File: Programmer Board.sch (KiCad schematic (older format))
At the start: 7 parts, among them J1 105-1103-001, J10 Conn_01x03, J11 105-1102-001, J12 105-1103-001, J2 Conn_01x03, J3 105-1102-001, J9 Conn_02x18_Odd_Even

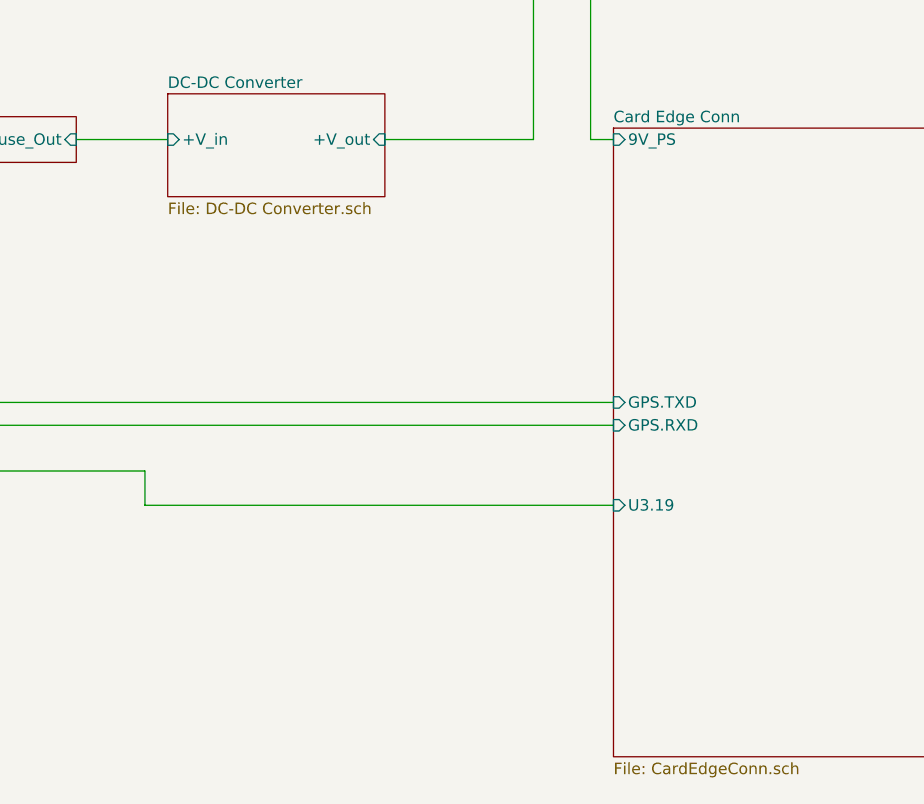
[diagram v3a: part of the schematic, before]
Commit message: Fixed DRC Errors
Fixed drc errors
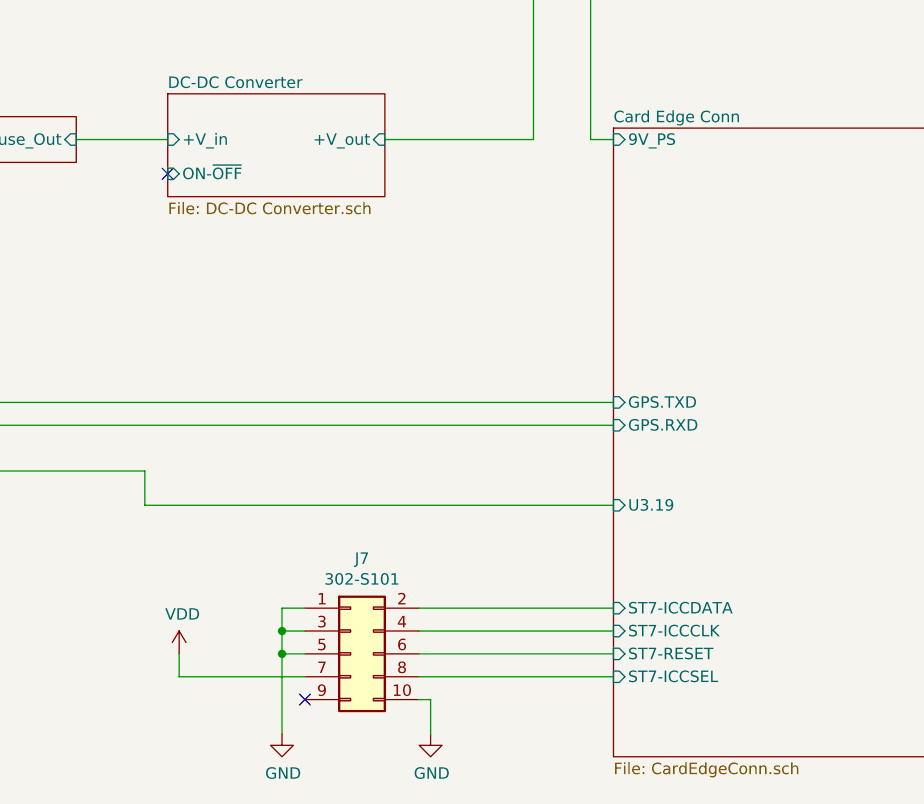
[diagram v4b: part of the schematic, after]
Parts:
- added J7: 302-S101, digikey-footprints:PinHeader_2x5_P2.54mm_Drill1.2mm, symbol Connector_Generic:Conn_02x05_Odd_Even
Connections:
- net GND: now also J7.1 (Pin_1), J7.10 (Pin_10), J7.3 (Pin_3), J7.5 (Pin_5)
- new net Card Edge Conn/ST7-ICCCLK: J7.4 (Pin_4)
- new net Card Edge Conn/ST7-ICCDATA: J7.2 (Pin_2)
- new net Card Edge Conn/ST7-ICCSEL: J7.8 (Pin_8)
- new net Card Edge Conn/ST7-RESET: J7.6 (Pin_6)
- new net VDD: J7.7 (Pin_7)
- no-connect marks 0 -> 2
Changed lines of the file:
@@
 Title "LMS6 Interface Board"
 Date "2020-10-17"
-Rev "6"
+Rev "7"
 Comp ""
-Comment1 "Rev 3: Changed sheet to US Letter"
-Comment2 "Rev 4: Fixed J9 hanging over border of sheet."
-Comment3 "Rev 5: Fixed J6 footprint and MPN info."
-Comment4 "Rev 6: Fixed footprint issues. Changed J9 connections for layout. Changed Y1."
+Comment1 "Rev 4: Fixed J9 hanging over border of sheet."
+Comment2 "Rev 5: Fixed J6 footprint and MPN info."
+Comment3 "Rev 6: Fixed footprint issues. Changed J9 connections for layout. Changed Y1."
+Comment4 "Rev 7: Ran DRC and fixed errors with flags to make rixon happy."
 $EndDescr
 $Sheet
@@
 F2 "+V_in" I L 4800 3300 50
 F3 "+V_out" I R 5750 3300 50
+F4 "ON-~OFF" I L 4800 3450 50
 $EndSheet
 $Comp
@@
 F22 "HEADER1.10" I R 9450 3600 50
 F23 "9V_PS" I L 6750 3300 50
+F24 "ST7-ICCSEL" I L 6750 5650 50
+F25 "ST7-ICCDATA" I L 6750 5350 50
+F26 "ST7-RESET" I L 6750 5550 50
+F27 "ST7-ICCCLK" I L 6750 5450 50
 $EndSheet
 Wire Wire Line
@@
 Text Label 900  3200 0    50   ~ 0
 -PS
+NoConn ~ 4800 3450
+$Comp
+L Connector_Generic:Conn_02x05_Odd_Even J?
+U 1 1 5F9DEBE9
+P 5600 5550
+AR Path="/5F7C6408/5F9DEBE9" Ref="J?"  Part="1"
+AR Path="/5F9DEBE9" Ref="J7"  Part="1"
+F 0 "J7" H 5650 5967 50  0000 C CNN
+F 1 "302-S101" H 5650 5876 50  0000 C CNN
+F 2 "digikey-footprints:PinHeader_2x5_P2.54mm_Drill1.2mm" H 5600 5550 50  0001 C CNN
+F 3 "http://www.on-shore.com/wp-content/uploads/2018/04/302-SXX1.pdf" H 5600 5550 50  0001 C CNN
+F 4 "302-S101" H 5600 5550 50  0001 C CNN "MPN"
+F 5 "On Shore Technology Inc." H 5600 5550 50  0001 C CNN "Maufacturer"
+	1    5600 5550
+	1    0    0    -1
+$EndComp
+$Comp
+L power:VDD #PWR0108
+U 1 1 5F9DEBF3
+P 4850 5550
+AR Path="/5F9DEBF3" Ref="#PWR0108"  Part="1"
+AR Path="/5F7BE189/5F9DEBF3" Ref="#PWR?"  Part="1"
+AR Path="/5F7C6408/5F9DEBF3" Ref="#PWR?"  Part="1"
+F 0 "#PWR0108" H 4850 5400 50  0001 C CNN
+F 1 "VDD" H 4865 5723 50  0000 C CNN
+F 2 "" H 4850 5550 50  0001 C CNN
+F 3 "" H 4850 5550 50  0001 C CNN
+	1    4850 5550
+	1    0    0    -1
+$EndComp
+Wire Wire Line
+	5400 5650 4850 5650
+Wire Wire Line
+	4850 5650 4850 5550
+$Comp
+L power:GND #PWR0109
+U 1 1 5F9DEBFB
+P 5300 5900
+AR Path="/5F9DEBFB" Ref="#PWR0109"  Part="1"
+AR Path="/5F7BE189/5F9DEBFB" Ref="#PWR?"  Part="1"
+AR Path="/5F7C6408/5F9DEBFB" Ref="#PWR?"  Part="1"
+F 0 "#PWR0109" H 5300 5650 50  0001 C CNN
+F 1 "GND" H 5305 5727 50  0000 C CNN
+F 2 "" H 5300 5900 50  0001 C CNN
+F 3 "" H 5300 5900 50  0001 C CNN
+	1    5300 5900
+	1    0    0    -1
+$EndComp
+Wire Wire Line
+	5300 5350 5400 5350
+Wire Wire Line
+	5300 5350 5300 5450
+Wire Wire Line
+	5400 5550 5300 5550
+Connection ~ 5300 5550
+Wire Wire Line
+	5300 5550 5300 5900
+Wire Wire Line
+	5400 5450 5300 5450
+Connection ~ 5300 5450
+Wire Wire Line
+	5300 5450 5300 5550
+$Comp
+L power:GND #PWR0110
+U 1 1 5F9DEC09
+P 5950 5900
+AR Path="/5F9DEC09" Ref="#PWR0110"  Part="1"
+AR Path="/5F7BE189/5F9DEC09" Ref="#PWR?"  Part="1"
+AR Path="/5F7C6408/5F9DEC09" Ref="#PWR?"  Part="1"
+F 0 "#PWR0110" H 5950 5650 50  0001 C CNN
+F 1 "GND" H 5955 5727 50  0000 C CNN
+F 2 "" H 5950 5900 50  0001 C CNN
+F 3 "" H 5950 5900 50  0001 C CNN
+	1    5950 5900
+	1    0    0    -1
+$EndComp
+Wire Wire Line
+	5900 5750 5950 5750
+Wire Wire Line
+	5950 5750 5950 5900
+NoConn ~ 5400 5750
+Wire Wire Line
+	5900 5350 6750 5350
+Wire Wire Line
+	5900 5450 6750 5450
+Wire Wire Line
+	5900 5550 6750 5550
+Wire Wire Line
+	5900 5650 6750 5650
 $EndSCHEMATC

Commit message: Final updates to REV B
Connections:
- net Card Edge Conn/HEADER1.1: now also J9.5 (Pin_5); no longer J9.31 (Pin_31)
- net Card Edge Conn/HEADER1.10: now also J9.35 (Pin_35); no longer J9.3 (Pin_3)
- net Card Edge Conn/HEADER1.2: now also J9.13 (Pin_13); no longer J9.23 (Pin_23)
- net Card Edge Conn/HEADER1.3: now also J9.15 (Pin_15); no longer J9.21 (Pin_21)
- net Card Edge Conn/HEADER1.4: now also J9.19 (Pin_19); no longer J9.15 (Pin_15)
- net Card Edge Conn/HEADER1.5: now also J9.17 (Pin_17); no longer J9.19 (Pin_19)
- net Card Edge Conn/HEADER1.6: now also J9.21 (Pin_21); no longer J9.17 (Pin_17)
- net Card Edge Conn/HEADER1.7: now also J9.25 (Pin_25); no longer J9.11 (Pin_11)
- net Card Edge Conn/HEADER1.9: now also J9.31 (Pin_31); no longer J9.7 (Pin_7)
- net Card Edge Conn/J5.2: now also J9.3 (Pin_3); no longer J9.35 (Pin_35)
- net Card Edge Conn/J5.3: now also J9.27 (Pin_27); no longer J9.9 (Pin_9)
- net Card Edge Conn/SW1.1: now also J9.9 (Pin_9); no longer J9.25 (Pin_25)
- net Card Edge Conn/SW1.2: now also J9.11 (Pin_11); no longer J9.27 (Pin_27)
- net Card Edge Conn/SW1.3: now also J9.29 (Pin_29); no longer J9.5 (Pin_5)
- net Card Edge Conn/SW1.4: now also J9.7 (Pin_7); no longer J9.29 (Pin_29)
- net Card Edge Conn/U21.20-DCLK: now also J9.1 (Pin_1); no longer J9.33 (Pin_33)
- net Card Edge Conn/U22.3: now also J9.23 (Pin_23); no longer J9.13 (Pin_13)
- net Card Edge Conn/U3.18: now also J9.33 (Pin_33); no longer J9.1 (Pin_1)
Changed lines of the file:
@@
 Title "LMS6 Interface Board"
 Date "2020-10-17"
-Rev "7"
+Rev "9"
 Comp ""
-Comment1 "Rev 4: Fixed J9 hanging over border of sheet."
-Comment2 "Rev 5: Fixed J6 footprint and MPN info."
-Comment3 "Rev 6: Fixed footprint issues. Changed J9 connections for layout. Changed Y1."
-Comment4 "Rev 7: Ran DRC and fixed errors with flags to make rixon happy."
+Comment1 "Rev 6: Fixed footprint issues. Changed J9 connections for layout. Changed Y1."
+Comment2 "Rev 7: Ran DRC and fixed errors with flags to make rixon happy."
+Comment3 "Rev 8: J5 changed to edge connector"
+Comment4 "Rev 9: J9 Modified to help with routing."
 $EndDescr
 $Sheet
@@
 F0 "Card Edge Conn" 50
 F1 "CardEdgeConn.sch" 50
-F2 "U21.20-DCLK" I R 9450 5100 50
-F3 "SW1.1" I R 9450 4700 50
+F2 "U21.20-DCLK" I R 9450 5200 50
+F3 "SW1.1" I R 9450 4800 50
 F4 "GPS.TXD" I L 6750 4450 50
 F5 "U22.3" I R 9450 4100 50
 F6 "J5.3" I R 9450 3900 50
-F7 "SW1.3" I R 9450 3700 50
-F8 "U3.18" I R 9450 3500 50
+F7 "SW1.3" I R 9450 3800 50
+F8 "U3.18" I R 9450 3600 50
 F9 "GPS.RXD" I L 6750 4550 50
 F10 "U3.19" I L 6750 4900 50
-F11 "SW1.2" I R 9450 4800 50
+F11 "SW1.2" I R 9450 4700 50
 F12 "SW1.4" I R 9450 4900 50
-F13 "J5.2" I R 9450 5200 50
+F13 "J5.2" I R 9450 5100 50
 F14 "HEADER1.1" I R 9450 5000 50
 F15 "HEADER1.2" I R 9450 4600 50
 F16 "HEADER1.3" I R 9450 4500 50
-F17 "HEADER1.4" I R 9450 4200 50
+F17 "HEADER1.4" I R 9450 4300 50
 F18 "HEADER1.5" I R 9450 4400 50
-F19 "HEADER1.6" I R 9450 4300 50
+F19 "HEADER1.6" I R 9450 4200 50
 F20 "HEADER1.7" I R 9450 4000 50
-F21 "HEADER1.9" I R 9450 3800 50
-F22 "HEADER1.10" I R 9450 3600 50
+F21 "HEADER1.9" I R 9450 3700 50
+F22 "HEADER1.10" I R 9450 3500 50
 F23 "9V_PS" I L 6750 3300 50
 F24 "ST7-ICCSEL" I L 6750 5650 50
@@
 L Connector_Generic:Conn_02x18_Odd_Even J9
 U 1 1 5F8F3B51
-P 9850 4300
-F 0 "J9" H 9900 5317 50  0000 C CNN
-F 1 "Conn_02x18_Odd_Even" H 9900 5226 50  0000 C CNN
-F 2 "Connector_PinHeader_2.54mm:PinHeader_2x18_P2.54mm_Vertical" H 9850 4300 50  0001 C CNN
-F 3 "https://drawings-pdf.s3.amazonaws.com/11636.pdf" H 9850 4300 50  0001 C CNN
-F 4 "Sullins Connector Solutions" H 9850 4300 50  0001 C CNN "Manufacturer"
-F 5 "PREC020DAAN-RC" H 9850 4300 50  0001 C CNN "MPN"
-	1    9850 4300
-	1    0    0    -1
+P 9850 4400
+F 0 "J9" H 9900 5417 50  0000 C CNN
+F 1 "Conn_02x18_Odd_Even" H 9900 5326 50  0000 C CNN
+F 2 "Connector_PinHeader_2.54mm:PinHeader_2x18_P2.54mm_Vertical" H 9850 4400 50  0001 C CNN
+F 3 "https://drawings-pdf.s3.amazonaws.com/11636.pdf" H 9850 4400 50  0001 C CNN
+F 4 "Sullins Connector Solutions" H 9850 4400 50  0001 C CNN "Manufacturer"
+F 5 "PREC020DAAN-RC" H 9850 4400 50  0001 C CNN "MPN"
+	1    9850 4400
+	1    0    0    1
 $EndComp
 $Comp
@@
 	5900 2350 5900 1350
 Wire Wire Line
-	9450 3500 9650 3500
-Wire Wire Line
-	9450 3600 9650 3600
-Wire Wire Line
 	9450 3700 9650 3700
 Wire Wire Line
@@
 Wire Wire Line
 	5900 5650 6750 5650
+Wire Wire Line
+	9450 3500 9650 3500
+Wire Wire Line
+	9450 3600 9650 3600
 $EndSCHEMATC

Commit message: Added product info and Schematic
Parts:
- J9: MPN PREC020DAAN-RC -> PREC018DAAN-RC
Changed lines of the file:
@@
 Title "LMS6 Interface Board"
 Date "2020-10-17"
-Rev "9"
+Rev "10"
 Comp ""
-Comment1 "Rev 6: Fixed footprint issues. Changed J9 connections for layout. Changed Y1."
-Comment2 "Rev 7: Ran DRC and fixed errors with flags to make rixon happy."
-Comment3 "Rev 8: J5 changed to edge connector"
-Comment4 "Rev 9: J9 Modified to help with routing."
+Comment1 "Rev 7: Ran DRC and fixed errors with flags to make rixon happy."
+Comment2 "Rev 8: J5 changed to edge connector"
+Comment3 "Rev 9: J9 Modified to help with routing."
+Comment4 "10/22/2020 Rev 10: Updated U3 part number and Manufact props"
 $EndDescr
 $Sheet
@@
 F 3 "https://drawings-pdf.s3.amazonaws.com/11636.pdf" H 9850 4400 50  0001 C CNN
 F 4 "Sullins Connector Solutions" H 9850 4400 50  0001 C CNN "Manufacturer"
-F 5 "PREC020DAAN-RC" H 9850 4400 50  0001 C CNN "MPN"
+F 5 "PREC018DAAN-RC" H 9850 4400 50  0001 C CNN "MPN"
 	1    9850 4400
 	1    0    0    1

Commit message: Rev C Board layout
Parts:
- added D2: LG R971-KN-1, LED_SMD:LED_0805_2012Metric_Pad1.15x1.40mm_HandSolder, symbol dk_LED-Indication-Discrete:LH_R974-LP-1
- added F1, F2: 750mA, Resistor_SMD:R_1812_4532Metric_Pad1.30x3.40mm_HandSolder, symbol Device:Polyfuse
- added JP3: JUMPER-SMT_3_1-NC, Jumpers:SMT-JUMPER_3_1-NC_TRACE_NO-SILK, symbol SparkFun-Jumpers:JUMPER-SMT_3_1-NC
- added R9: 280, Resistor_SMD:R_0805_2012Metric_Pad1.20x1.40mm_HandSolder, symbol Device:R_US
- E1: renamed from J3; value 105-1102-001 -> 575-4; footprint digikey-footprints:Test_Jack_Horiz -> LMS-6_Interface_Board:575_Banana_Jack; DK_Datasheet_Link https://belfuse.com/resources/Johnson/drawings/dr-105110100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 -> http://keyelco.com/userAssets/file/M65p111.pdf; Digi-Key_PN J576-ND -> 36-575-4-ND; MPN 105-1102-001 -> 575-4
- E2: renamed from J1; value 105-1103-001 -> 575-4; footprint digikey-footprints:Test_Jack_Horiz -> LMS-6_Interface_Board:575_Banana_Jack; DK_Datasheet_Link https://belfuse.com/resources/Johnson/drawings/dr-105110100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 -> http://keyelco.com/userAssets/file/M65p111.pdf; Digi-Key_PN J577-ND -> 36-575-4-ND
- E3: renamed from J11; value 105-1102-001 -> 575-4; footprint digikey-footprints:Test_Jack_Horiz -> LMS-6_Interface_Board:575_Banana_Jack; DK_Datasheet_Link https://belfuse.com/resources/Johnson/drawings/dr-105110100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 -> http://keyelco.com/userAssets/file/M65p111.pdf; Digi-Key_PN J576-ND -> 36-575-4-ND; MPN 105-1102-001 -> 575-4
- E4: renamed from J12; value 105-1103-001 -> 575-4; footprint digikey-footprints:Test_Jack_Horiz -> LMS-6_Interface_Board:575_Banana_Jack; MPN 105-1103-001 -> 36-575-4-ND
- J7: footprint digikey-footprints:PinHeader_2x5_P2.54mm_Drill1.2mm -> digikey-footprints:PinHeader_2x5_P2.54mm_Drill1.02mm
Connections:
- net eFuse/eFuse_In is gone; now on net DC-DC Converter/+V_in: J2.2 (Pin_2)
- net +PS: now also F1.1; no longer E1.1
- net Card Edge Conn/U3.19: now also JP3.2
- net GND: now also R9.2
- net at J10.1 (Pin_1): now also F2.1; no longer E3.1
- net USB to UART/+5_USB renamed +5_USB
- net +5_USB: now also D2.2
- new net: E1.1, F1.2
- new net: E3.1, F2.2
- new net: D2.1, R9.1
- new net sheet5FC8868D/RXD: JP3.1
- new net sheet5FC8868D/TXD: JP3.3
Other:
- note removed: "External power source select. \nJumper 1-2 for banana jacks. \nJumper 2-3 for USB power."
- moved on the sheet: E1, E2, E3, J2

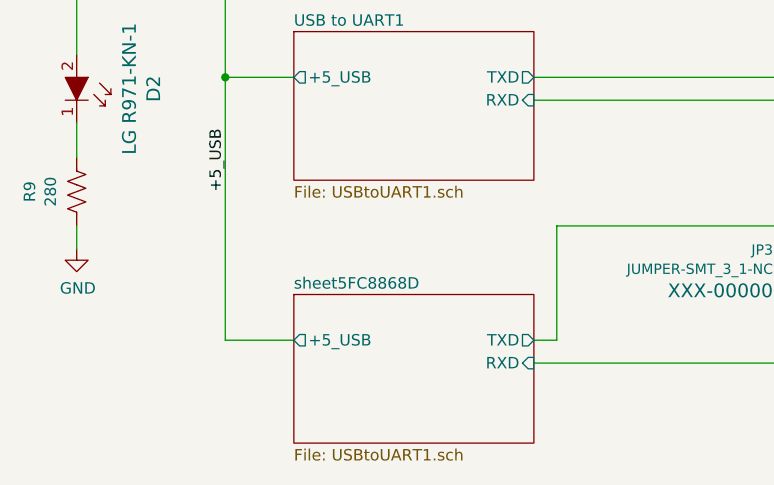
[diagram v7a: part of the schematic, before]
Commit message: Rev C PCB as sent to fabrication
REV C PCB as sent to fabrication with clean up directory structure.
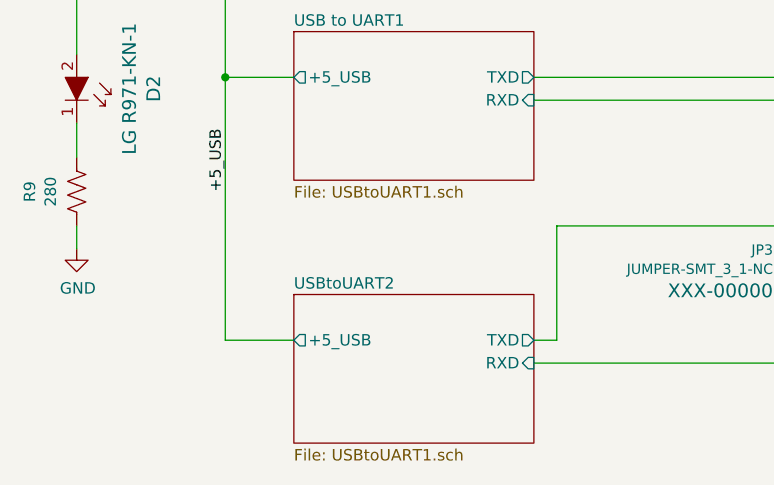
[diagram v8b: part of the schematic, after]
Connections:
- net sheet5FC8868D/RXD renamed USBtoUART2/RXD
- net sheet5FC8868D/TXD renamed USBtoUART2/TXD
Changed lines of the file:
@@
 Sheet 1 5
 Title "LMS6 Interface Board"
-Date "2020-10-17"
-Rev "10"
+Date "2020-11-27"
+Rev "11"
 Comp ""
-Comment1 "Rev 7: Ran DRC and fixed errors with flags to make rixon happy."
-Comment2 "Rev 8: J5 changed to edge connector"
-Comment3 "Rev 9: J9 Modified to help with routing."
-Comment4 "10/22/2020 Rev 10: Updated U3 part number and Manufact props"
+Comment1 "Rev 8: J5 changed to edge connector"
+Comment2 "Rev 9: J9 Modified to help with routing."
+Comment3 "10/22/2020 Rev 10: Updated U3 part number and Manufact props"
+Comment4 "11/27/2020 Rev 11: Implemented PCB Rev C Changes"
 $EndDescr
 $Sheet
@@
 S 2100 5400 1050 650
 U 5FC88692
-F0 "sheet5FC8868D" 50
+F0 "USBtoUART2" 50
 F1 "USBtoUART1.sch" 50
 F2 "+5_USB" O L 2100 5600 50
